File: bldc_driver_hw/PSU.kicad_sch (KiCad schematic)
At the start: 48 parts, among them U14 TPS54360DDA, U3 TPS562201DDCR, U4 AMS1117-3.3

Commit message: finished
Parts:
- C16, C17: value 47uF -> 22uF
- D4, L1, L4, R13, R14, R15, TP15, TP38, TP5, TP6, TP7, TP8, TP9, U14, U3: now left out of the parts list
- R11: now fitted; now left out of the parts list
- R18: LCSC (none) -> C25803; now fitted
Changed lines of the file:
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@@
 					(size 1.27 1.27)
 				)
+				(hide yes)
 			)
 		)
@@
 					(size 1.27 1.27)
 				)
+				(hide yes)
 			)
 		)
@@
 					(size 1.27 1.27)
 				)
+				(hide yes)
 			)
 		)
@@
 		(unit 1)
 		(exclude_from_sim no)
-		(in_bom yes)
+		(in_bom no)
 		(on_board yes)
 		(dnp no)
@@
 		(unit 1)
 		(exclude_from_sim no)
-		(in_bom yes)
+		(in_bom no)
 		(on_board yes)
 		(dnp no)
@@
 		(unit 1)
 		(exclude_from_sim no)
-		(in_bom yes)
+		(in_bom no)
 		(on_board yes)
 		(dnp no)
@@
 		(unit 1)
 		(exclude_from_sim no)
-		(in_bom yes)
+		(in_bom no)
 		(on_board yes)
 		(dnp no)
@@
 					(size 1.27 1.27)
 				)
+				(hide yes)
 			)
 		)
@@
 		(in_bom yes)
 		(on_board yes)
-		(dnp yes)
+		(dnp no)
 		(fields_autoplaced yes)
 		(property "Reference" "R18"
@@
 			)
 		)
+		(property "LCSC" "C25803"
+			(at 59.69 43.18 0)
+			(effects
+				(font
+					(size 1.27 1.27)
+				)
+			)
+		)
 		(pin "1"
 		)
@@
 					(size 1.27 1.27)
 				)
+				(hide yes)
 			)
 		)
@@
 					(size 1.27 1.27)
 				)
+				(hide yes)
 			)
 		)
@@
 		(unit 1)
 		(exclude_from_sim no)
-		(in_bom yes)
+		(in_bom no)
 		(on_board yes)
 		(dnp no)
@@
 		(unit 1)
 		(exclude_from_sim no)
-		(in_bom yes)
+		(in_bom no)
 		(on_board yes)
 		(dnp no)
@@
 		(unit 1)
 		(exclude_from_sim no)
-		(in_bom yes)
+		(in_bom no)
 		(on_board yes)
 		(dnp no)
@@
 					(size 1.27 1.27)
 				)
+				(hide yes)
 			)
 		)
@@
 		(unit 1)
 		(exclude_from_sim no)
-		(in_bom yes)
+		(in_bom no)
 		(on_board yes)
 		(dnp no)
@@
 					(size 1.27 1.27)
 				)
+				(hide yes)
 			)
 		)
@@
 					(size 1.27 1.27)
 				)
+				(hide yes)
 			)
 		)
@@
 					(size 1.27 1.27)
 				)
+				(hide yes)
 			)
 		)
@@
 		(unit 1)
 		(exclude_from_sim no)
-		(in_bom yes)
+		(in_bom no)
 		(on_board yes)
 		(dnp no)
@@
 		(unit 1)
 		(exclude_from_sim no)
-		(in_bom yes)
+		(in_bom no)
 		(on_board yes)
 		(dnp no)
@@
 					(size 1.27 1.27)
 				)
+				(hide yes)
 			)
 		)
@@
 		(unit 1)
 		(exclude_from_sim no)
-		(in_bom yes)
+		(in_bom no)
 		(on_board yes)
 		(dnp no)
@@
 			)
 		)
-		(property "Value" "47uF"
+		(property "Value" "22uF"
 			(at 182.88 36.8362 0)
 			(effects
@@
 		)
 		(property "LCSC" "C45783"
-			(at 180.34 35.56 0)
+			(at 182.88 38.1062 0)
 			(effects
 				(font
 					(size 1.27 1.27)
 				)
+				(justify left)
+				(hide yes)
 			)
 		)
@@
 					(size 1.27 1.27)
 				)
+				(hide yes)
 			)
 		)
@@
 		(unit 1)
 		(exclude_from_sim no)
-		(in_bom yes)
+		(in_bom no)
 		(on_board yes)
-		(dnp yes)
+		(dnp no)
 		(fields_autoplaced yes)
 		(property "Reference" "R11"
@@
 		(unit 1)
 		(exclude_from_sim no)
-		(in_bom yes)
+		(in_bom no)
 		(on_board yes)
 		(dnp no)
@@
 					(size 1.27 1.27)
 				)
+				(hide yes)
 			)
 		)
@@
 		(unit 1)
 		(exclude_from_sim no)
-		(in_bom yes)
+		(in_bom no)
 		(on_board yes)
 		(dnp no)
@@
 			)
 		)
-		(property "Value" "47uF"
+		(property "Value" "22uF"
 			(at 170.18 36.8362 0)
 			(effects
@@
 		)
 		(property "LCSC" "C45783"
-			(at 167.64 35.56 0)
+			(at 170.18 38.1062 0)
 			(effects
 				(font
 					(size 1.27 1.27)
 				)
+				(justify left)
+				(hide yes)
 			)
 		)
@@
 		(unit 1)
 		(exclude_from_sim no)
-		(in_bom yes)
+		(in_bom no)
 		(on_board yes)
 		(dnp no)
@@
 					(size 1.27 1.27)
 				)
+				(hide yes)
 			)
 		)
@@
 					(size 1.27 1.27)
 				)
+				(hide yes)
 			)
 		)
@@
 					(size 1.27 1.27)
 				)
+				(hide yes)
 			)
 		)
@@
 					(size 1.27 1.27)
 				)
+				(hide yes)
 			)
 		)
@@
 		(unit 1)
 		(exclude_from_sim no)
-		(in_bom yes)
+		(in_bom no)
 		(on_board yes)
 		(dnp no)

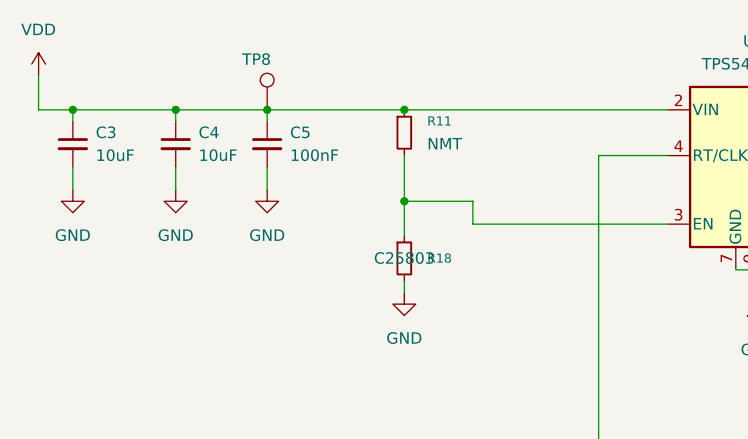
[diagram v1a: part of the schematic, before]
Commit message: Changed size of capacitors at input 48V dc converter
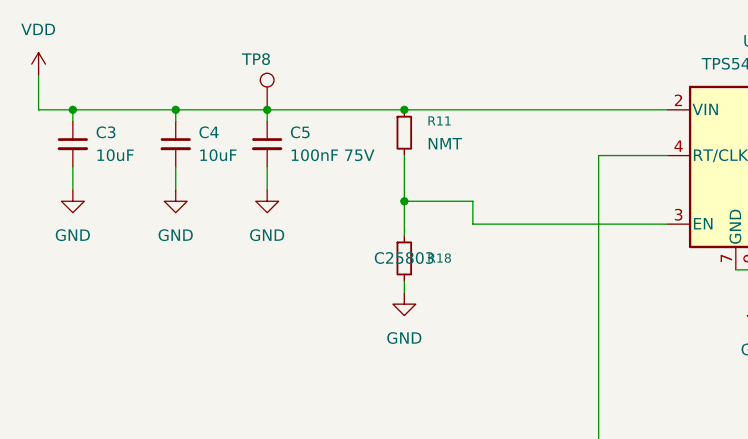
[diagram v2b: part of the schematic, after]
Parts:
- C3, C4: footprint Capacitor_SMD:C_0805_2012Metric -> Capacitor_SMD:C_1210_3225Metric; LCSC C440198 -> (none)
- C5: value 100nF -> 100nF 75V; footprint Capacitor_SMD:C_0603_1608Metric -> Capacitor_SMD:C_0805_2012Metric; LCSC C14663 -> (none)
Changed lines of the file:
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@@
 	)
 	(symbol
+		(lib_id "Device:C_Small")
+		(at 34.29 30.48 0)
+		(unit 1)
+		(exclude_from_sim no)
+		(in_bom yes)
+		(on_board yes)
+		(dnp no)
+		(fields_autoplaced yes)
+		(property "Reference" "C4"
+			(at 36.83 29.2162 0)
+			(effects
+				(font
+					(size 1.27 1.27)
+				)
+				(justify left)
+			)
+		)
+		(property "Value" "10uF"
+			(at 36.83 31.7562 0)
+			(effects
+				(font
+					(size 1.27 1.27)
+				)
+				(justify left)
+			)
+		)
+		(property "Footprint" "Capacitor_SMD:C_1210_3225Metric"
+			(at 34.29 30.48 0)
+			(effects
+				(font
+					(size 1.27 1.27)
+				)
+				(hide yes)
+			)
+		)
+		(property "Datasheet" "~"
+			(at 34.29 30.48 0)
+			(effects
+				(font
+					(size 1.27 1.27)
+				)
+				(hide yes)
+			)
+		)
+		(property "Description" "Unpolarized capacitor, small symbol"
+			(at 34.29 30.48 0)
+			(effects
+				(font
+					(size 1.27 1.27)
+				)
+				(hide yes)
+			)
+		)
+		(property "LCSC" ""
+			(at 34.29 30.48 0)
+			(effects
+				(font
+					(size 1.27 1.27)
+				)
+				(hide yes)
+			)
+		)
+		(pin "2"
+		)
+		(pin "1"
+		)
+		(instances
+			(project "bldc_driver_hw"
+				(path "/7f946e06-72d3-4343-93fe-84e8bb5001be/d7c582d1-04cb-4ff4-bbcf-fae814c237ea"
+					(reference "C4")
+					(unit 1)
+				)
+			)
+		)
+	)
+	(symbol
 		(lib_id "Regulator_Switching:TPS562200")
 		(at 82.55 102.87 0)
@@
 			)
 		)
-		(property "Value" "100nF"
+		(property "Value" "100nF 75V"
 			(at 46.99 31.7562 0)
 			(effects
@@
 			)
 		)
-		(property "Footprint" "Capacitor_SMD:C_0603_1608Metric"
+		(property "Footprint" "Capacitor_SMD:C_0805_2012Metric"
 			(at 44.45 30.48 0)
 			(effects
@@
 			)
 		)
-		(property "LCSC" "C14663"
+		(property "LCSC" ""
 			(at 44.45 30.48 0)
 			(effects
@@
 	(symbol
 		(lib_id "Device:C_Small")
-		(at 34.29 30.48 0)
-		(unit 1)
-		(exclude_from_sim no)
-		(in_bom yes)
-		(on_board yes)
-		(dnp no)
-		(fields_autoplaced yes)
-		(property "Reference" "C4"
-			(at 36.83 29.2162 0)
-			(effects
-				(font
-					(size 1.27 1.27)
-				)
-				(justify left)
-			)
-		)
-		(property "Value" "10uF"
-			(at 36.83 31.7562 0)
-			(effects
-				(font
-					(size 1.27 1.27)
-				)
-				(justify left)
-			)
-		)
-		(property "Footprint" "Capacitor_SMD:C_0805_2012Metric"
-			(at 34.29 30.48 0)
-			(effects
-				(font
-					(size 1.27 1.27)
-				)
-				(hide yes)
-			)
-		)
-		(property "Datasheet" "~"
-			(at 34.29 30.48 0)
-			(effects
-				(font
-					(size 1.27 1.27)
-				)
-				(hide yes)
-			)
-		)
-		(property "Description" "Unpolarized capacitor, small symbol"
-			(at 34.29 30.48 0)
-			(effects
-				(font
-					(size 1.27 1.27)
-				)
-				(hide yes)
-			)
-		)
-		(property "LCSC" "C440198"
-			(at 34.29 30.48 0)
-			(effects
-				(font
-					(size 1.27 1.27)
-				)
-				(hide yes)
-			)
-		)
-		(pin "2"
-		)
-		(pin "1"
-		)
-		(instances
-			(project "bldc_driver_hw"
-				(path "/7f946e06-72d3-4343-93fe-84e8bb5001be/d7c582d1-04cb-4ff4-bbcf-fae814c237ea"
-					(reference "C4")
-					(unit 1)
-				)
-			)
-		)
-	)
-	(symbol
-		(lib_id "Device:C_Small")
 		(at 242.57 149.86 0)
 		(unit 1)
@@
 			)
 		)
-		(property "Footprint" "Capacitor_SMD:C_0805_2012Metric"
+		(property "Footprint" "Capacitor_SMD:C_1210_3225Metric"
 			(at 22.86 30.48 0)
 			(effects
@@
 			)
 		)
-		(property "LCSC" "C440198"
+		(property "LCSC" ""
 			(at 22.86 30.48 0)
 			(effects

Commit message: changed hrtim to tim1
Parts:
- C3, C4: now left out of the parts list
- C5: LCSC (none) -> C28233
- L4: LCSC LMLP0506M4R7DTAS -> (none)
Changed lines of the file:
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@@
 		(unit 1)
 		(exclude_from_sim no)
-		(in_bom yes)
+		(in_bom no)
 		(on_board yes)
 		(dnp no)
@@
 			)
 		)
-		(property "LCSC" ""
+		(property "LCSC" "C28233"
 			(at 44.45 30.48 0)
 			(effects
@@
 			)
 		)
-		(property "Description" "5A sat"
-			(at 107.95 100.33 0)
-			(effects
-				(font
-					(size 1.27 1.27)
-				)
-				(hide yes)
-			)
-		)
-		(property "LCSC" "LMLP0506M4R7DTAS"
+		(property "Description" "LMLP0506M4R7DTAS 5A sat"
 			(at 107.95 100.33 0)
 			(effects
@@
 		(unit 1)
 		(exclude_from_sim no)
-		(in_bom yes)
+		(in_bom no)
 		(on_board yes)
 		(dnp no)
